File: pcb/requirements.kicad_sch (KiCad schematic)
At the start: 14 parts

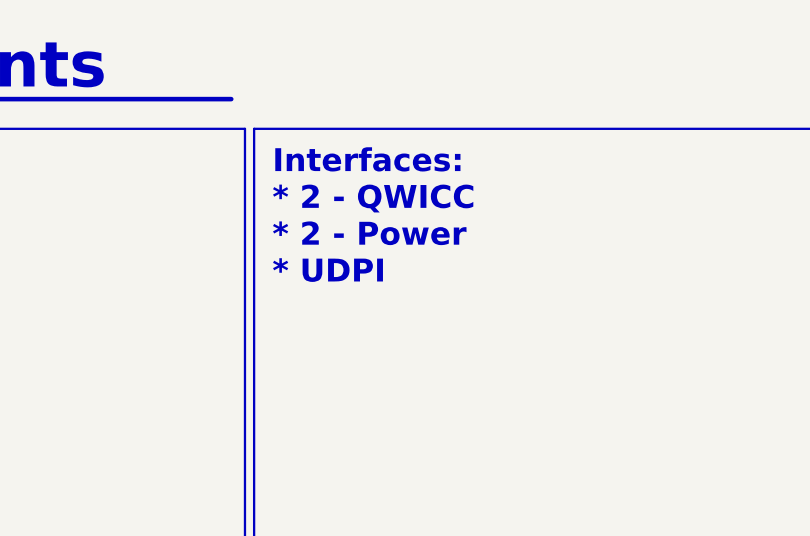
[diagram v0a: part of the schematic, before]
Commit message: Removed power connectors
Removed power connector as 5v is not necessary.
Added 100uF caps to power
Added TVS to I2C and VOUT
Rerouted entire board
Adjusted silkscreen
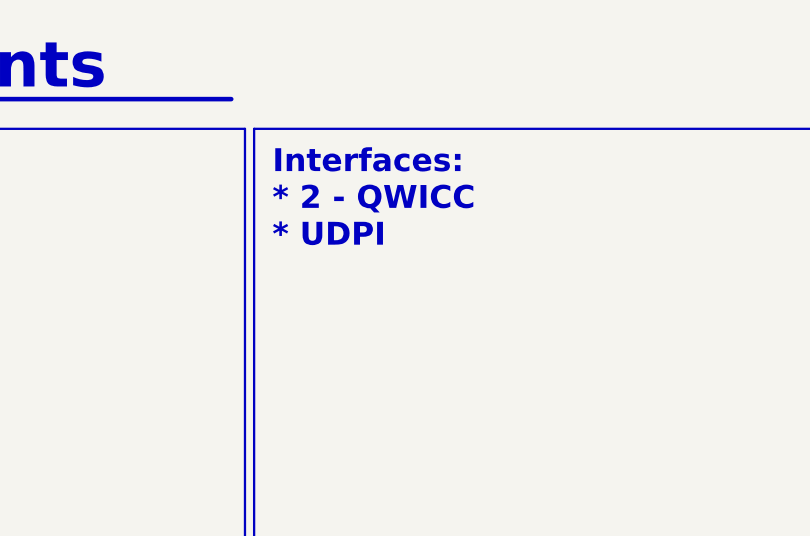
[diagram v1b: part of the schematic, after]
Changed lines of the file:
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@@
 		)
 	)
-	(text_box "Interfaces:\n* 2 - QWICC\n* 2 - Power\n* UDPI"
+	(text_box "Interfaces:\n* 2 - QWICC\n* UDPI"
 		(exclude_from_sim yes)
 		(at 189.992 25.4 0)

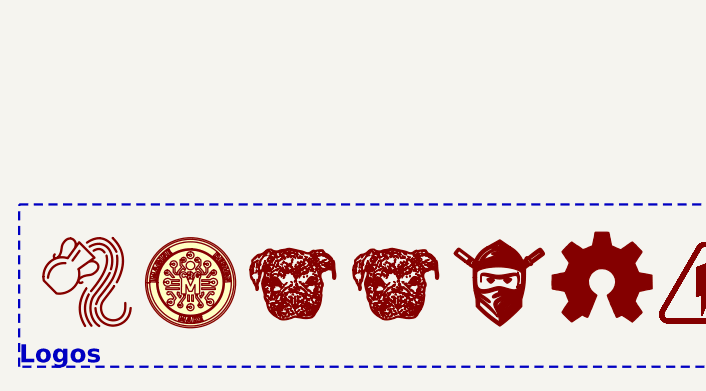
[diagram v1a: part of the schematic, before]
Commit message: Collapsed UPDI and Serial
Added indicator LEDs
Rerouted
Cleaned up silkscreen
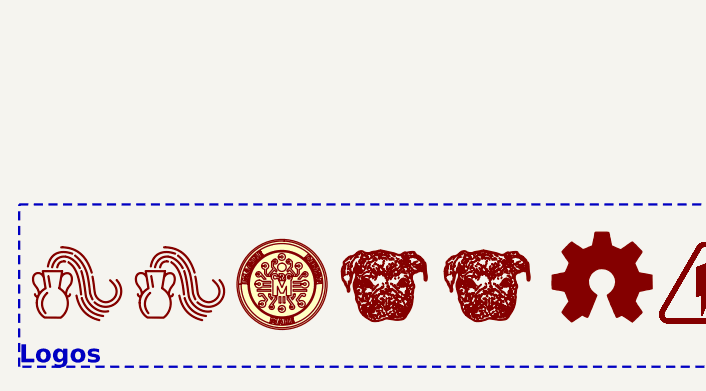
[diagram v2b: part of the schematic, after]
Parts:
- removed LOGO6: ~, CRGM Logos:FNWW Face 5mm, symbol CRGM Logos:FNWW Face
- added LOGO7: ~, CRGM Logos:Aquarius Logo 3.5mm, symbol CRGM Logos:Aquarius Logo
- LOGO2: footprint CRGM Logos:Roxy 3.5mm -> CRGM Logos:Roxy 4mm

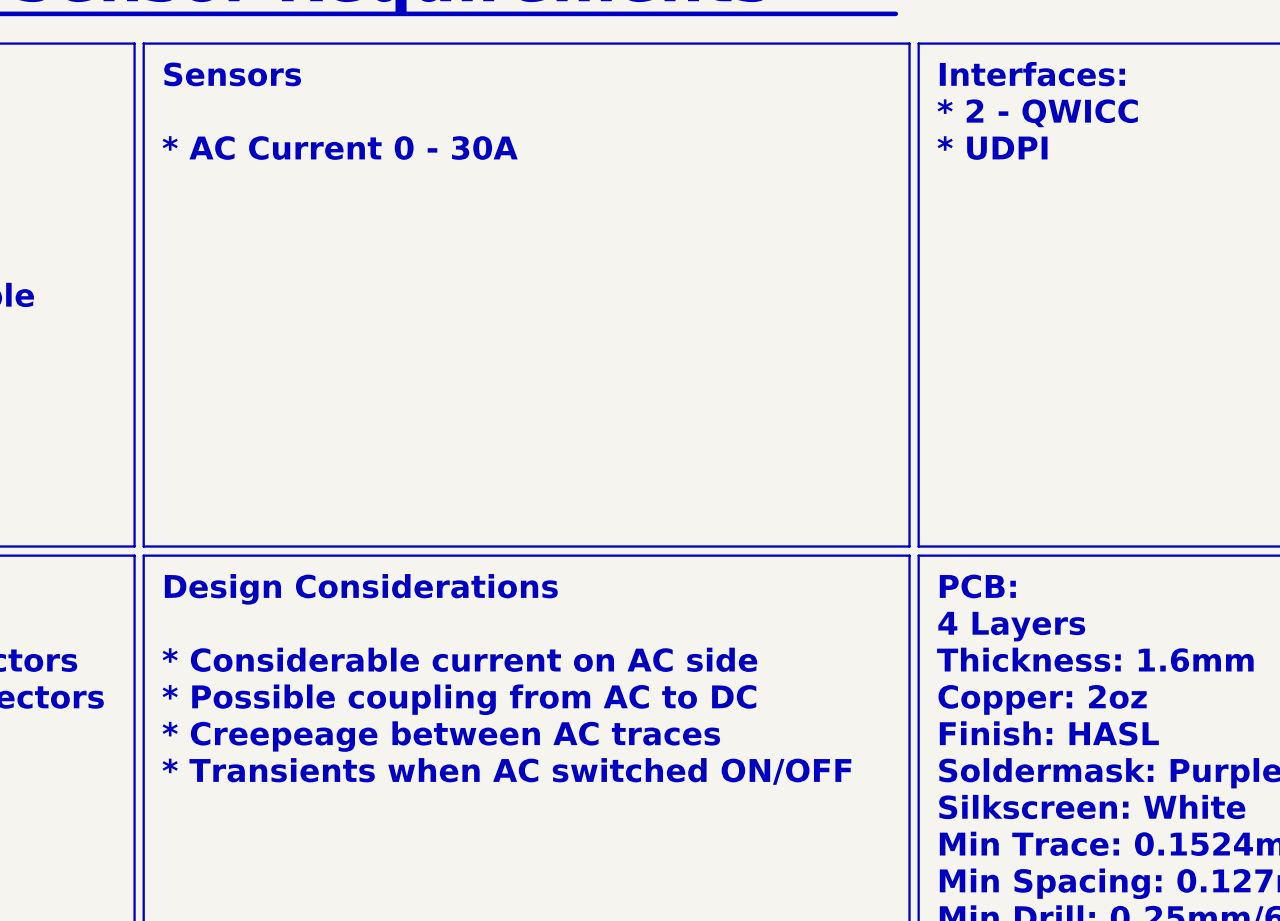
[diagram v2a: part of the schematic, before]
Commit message: Fixed MCU Footprint
Updated renders
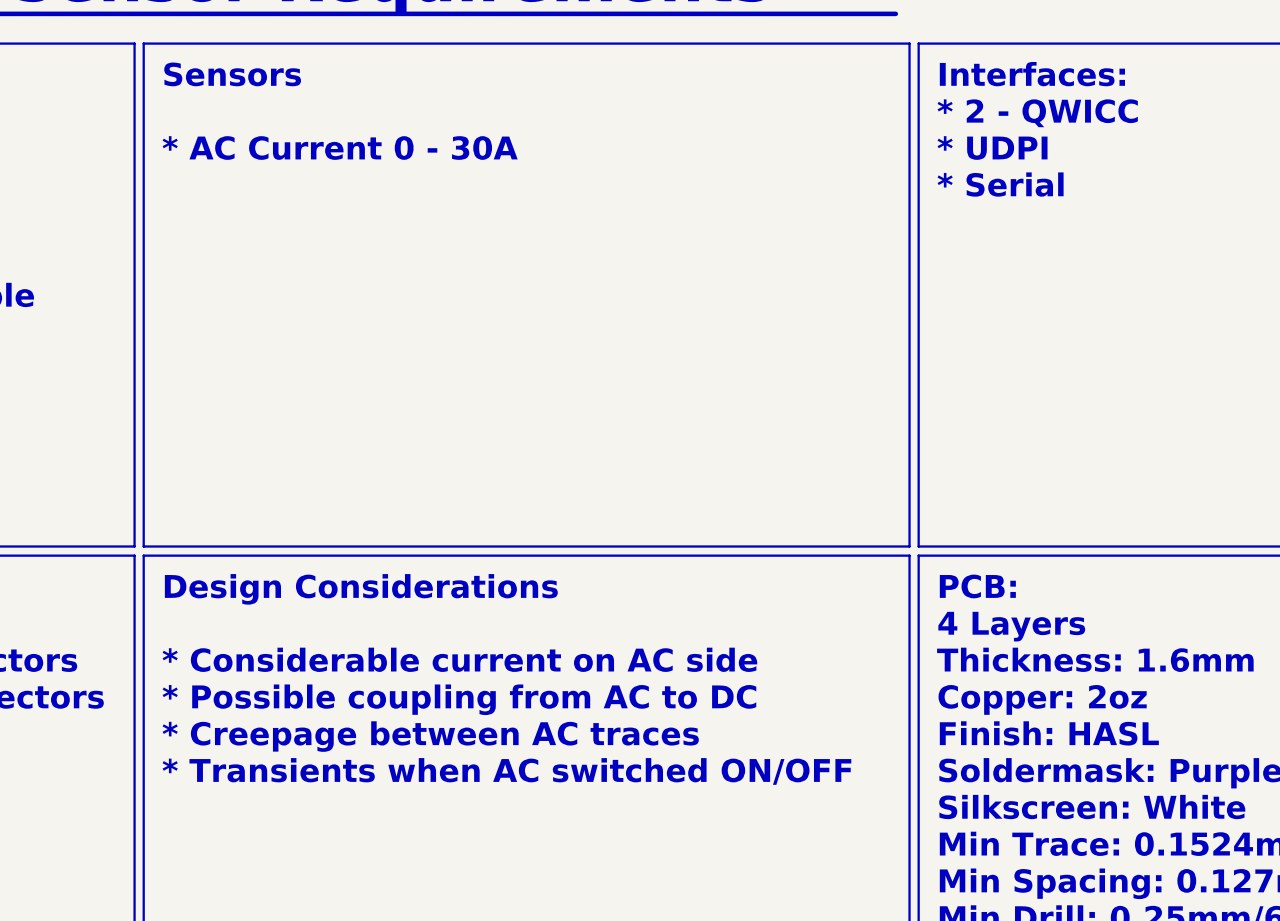
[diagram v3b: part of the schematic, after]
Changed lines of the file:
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@@
 		)
 	)
-	(text_box "Interfaces:\n* 2 - QWICC\n* UDPI"
+	(text_box "Interfaces:\n* 2 - QWICC\n* UDPI\n* Serial"
 		(exclude_from_sim yes)
 		(at 189.992 25.4 0)
@@
 		)
 	)
-	(text_box "Design Considerations\n\n* Considerable current on AC side\n* Possible coupling from AC to DC\n* Creepeage between AC traces\n* Transients when AC switched ON/OFF"
+	(text_box "Design Considerations\n\n* Considerable current on AC side\n* Possible coupling from AC to DC\n* Creepage between AC traces\n* Transients when AC switched ON/OFF"
 		(exclude_from_sim yes)
 		(at 103.886 82.296 0)
@@
 			)
 		)
-		(property "Sim.Enable" ""
-			(at 21.59 186.69 0)
-			(effects
-				(font
-					(size 1.27 1.27)
-				)
-				(hide yes)
-			)
-		)
 		(instances
 			(project "current-module"
@@
 			)
 		)
-		(property "Sim.Enable" ""
-			(at 80.01 186.5 0)
-			(effects
-				(font
-					(size 1.27 1.27)
-				)
-				(hide yes)
-			)
-		)
 		(instances
 			(project "current-module"
@@
 		)
 		(property "Mouser" ""
-			(at 67.31 186.69 0)
-			(effects
-				(font
-					(size 1.27 1.27)
-				)
-				(hide yes)
-			)
-		)
-		(property "Sim.Enable" ""
 			(at 67.31 186.69 0)
 			(effects
@@
 			)
 		)
-		(property "Sim.Enable" ""
-			(at 114.3 186.5 0)
-			(effects
-				(font
-					(size 1.27 1.27)
-				)
-				(hide yes)
-			)
-		)
 		(instances
 			(project "current-module"
@@
 		(property "MPN" ""
 			(at 154.94 175.26 0)
-			(effects
-				(font
-					(size 1.27 1.27)
-				)
-				(hide yes)
-			)
-		)
-		(property "Sim.Enable" ""
-			(at 154.94 175.26 90)
 			(effects
 				(font
@@
 			)
 		)
-		(property "Sim.Enable" ""
-			(at 125.73 186.5 0)
-			(effects
-				(font
-					(size 1.27 1.27)
-				)
-				(hide yes)
-			)
-		)
 		(instances
 			(project "current-module"
@@
 		)
 		(property "Mouser" ""
-			(at 44.45 186.69 0)
-			(effects
-				(font
-					(size 1.27 1.27)
-				)
-				(hide yes)
-			)
-		)
-		(property "Sim.Enable" ""
 			(at 44.45 186.69 0)
 			(effects
@@
 			)
 		)
-		(property "Sim.Enable" ""
-			(at 91.44 186.5 0)
-			(effects
-				(font
-					(size 1.27 1.27)
-				)
-				(hide yes)
-			)
-		)
 		(instances
 			(project "current-module"
@@
 		(property "MPN" ""
 			(at 154.94 185.42 0)
-			(effects
-				(font
-					(size 1.27 1.27)
-				)
-				(hide yes)
-			)
-		)
-		(property "Sim.Enable" ""
-			(at 154.94 185.42 90)
 			(effects
 				(font
@@
 			)
 		)
-		(property "Sim.Enable" ""
-			(at 154.94 170.18 90)
-			(effects
-				(font
-					(size 1.27 1.27)
-				)
-				(hide yes)
-			)
-		)
 		(pin "1"
 		)
@@
 			)
 		)
-		(property "Sim.Enable" ""
-			(at 102.87 186.5 0)
-			(effects
-				(font
-					(size 1.27 1.27)
-				)
-				(hide yes)
-			)
-		)
 		(instances
 			(project "current-module"
@@
 		)
 		(property "Mouser" ""
-			(at 55.88 186.69 0)
-			(effects
-				(font
-					(size 1.27 1.27)
-				)
-				(hide yes)
-			)
-		)
-		(property "Sim.Enable" ""
 			(at 55.88 186.69 0)
 			(effects
@@
 			)
 		)
-		(property "Sim.Enable" ""
-			(at 33.02 186.69 0)
-			(effects
-				(font
-					(size 1.27 1.27)
-				)
-				(hide yes)
-			)
-		)
 		(instances
 			(project "current-module"
@@
 			(effects
 				(font
-					(size 1.27 1.27)
-				)
-				(hide yes)
-			)
-		)
-		(property "Sim.Enable" ""
-			(at 154.94 180.34 90)
-			(effects
-				(font
